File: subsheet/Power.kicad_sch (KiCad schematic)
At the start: 27 parts, among them J501 Barrel_Jack, J502 PWR_IN, J503 ALTERNATE, Q501 DTC114E, Q502 DTC114E, U501 TPS2552DBV, U502 TPS2552DBV

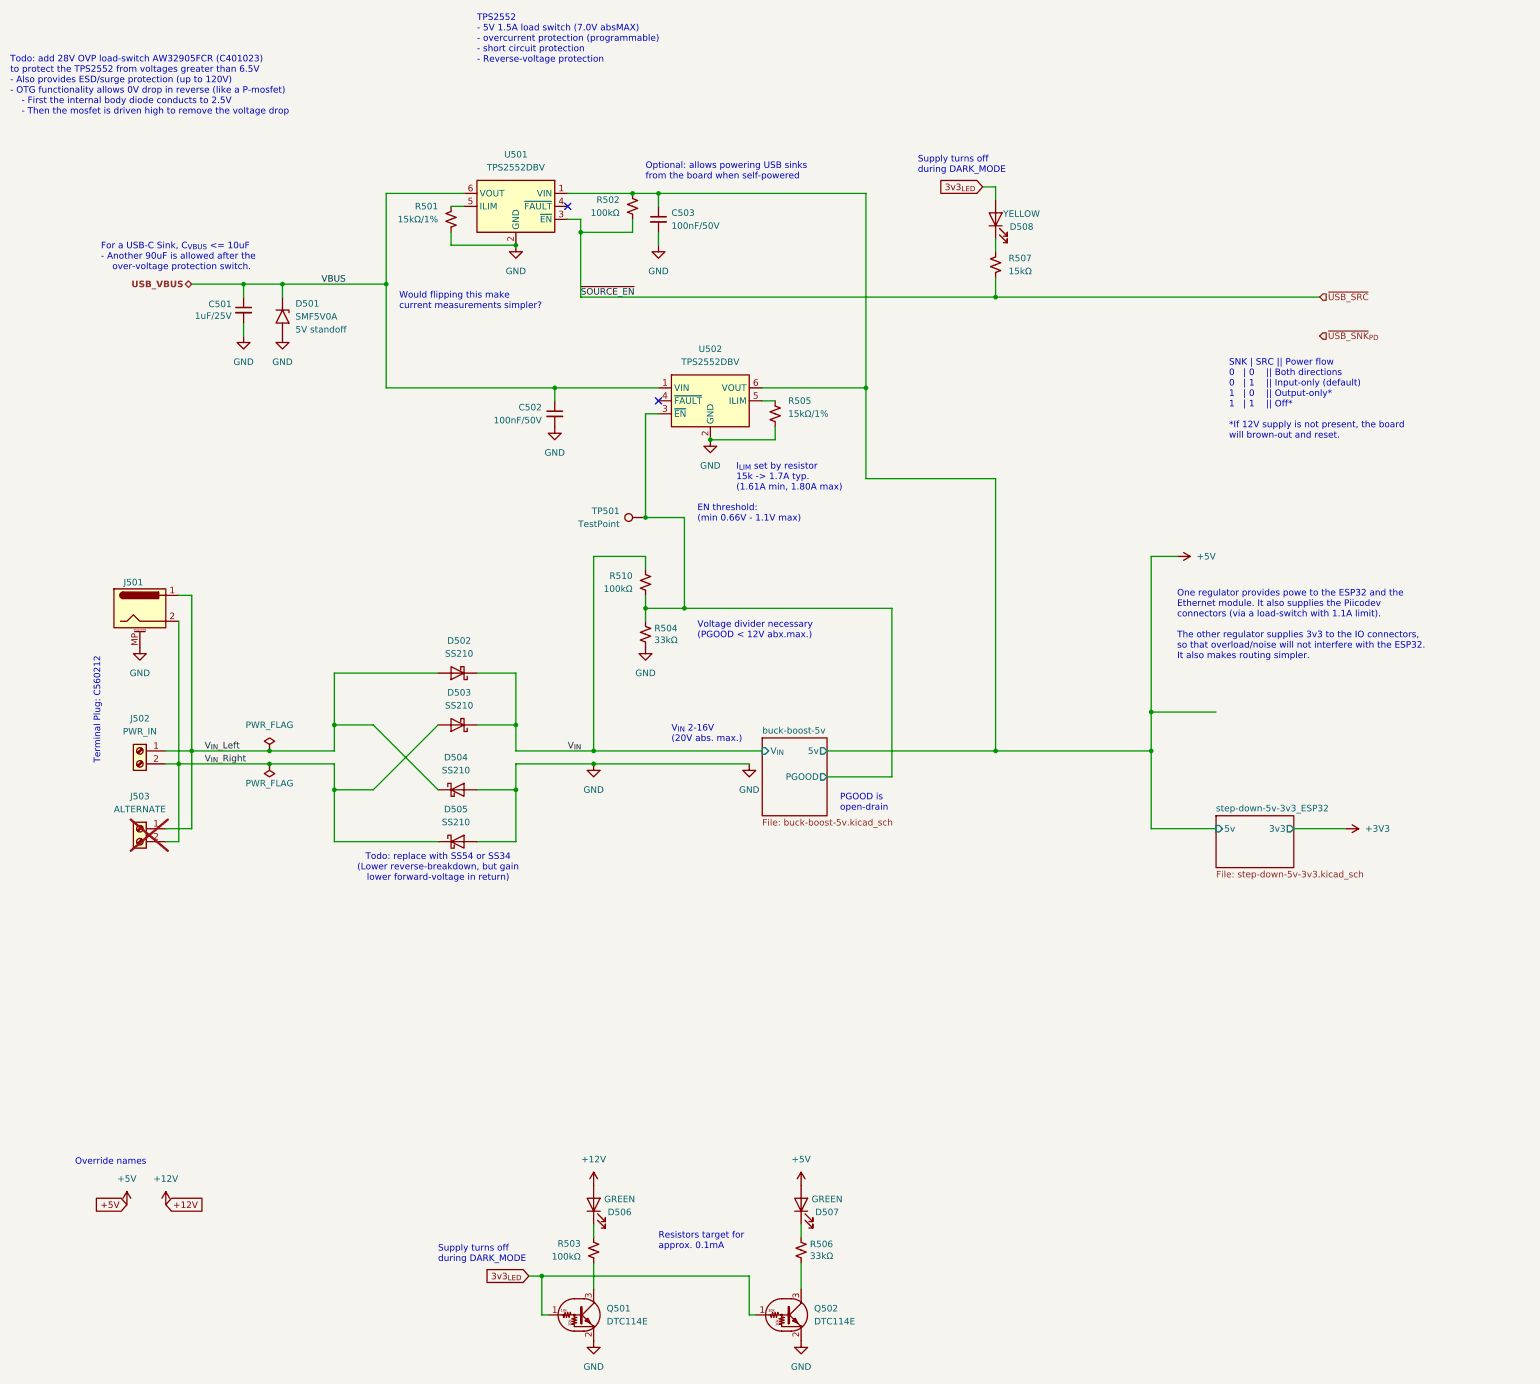
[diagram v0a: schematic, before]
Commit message: Removed USB-PD circuit - simplifies board
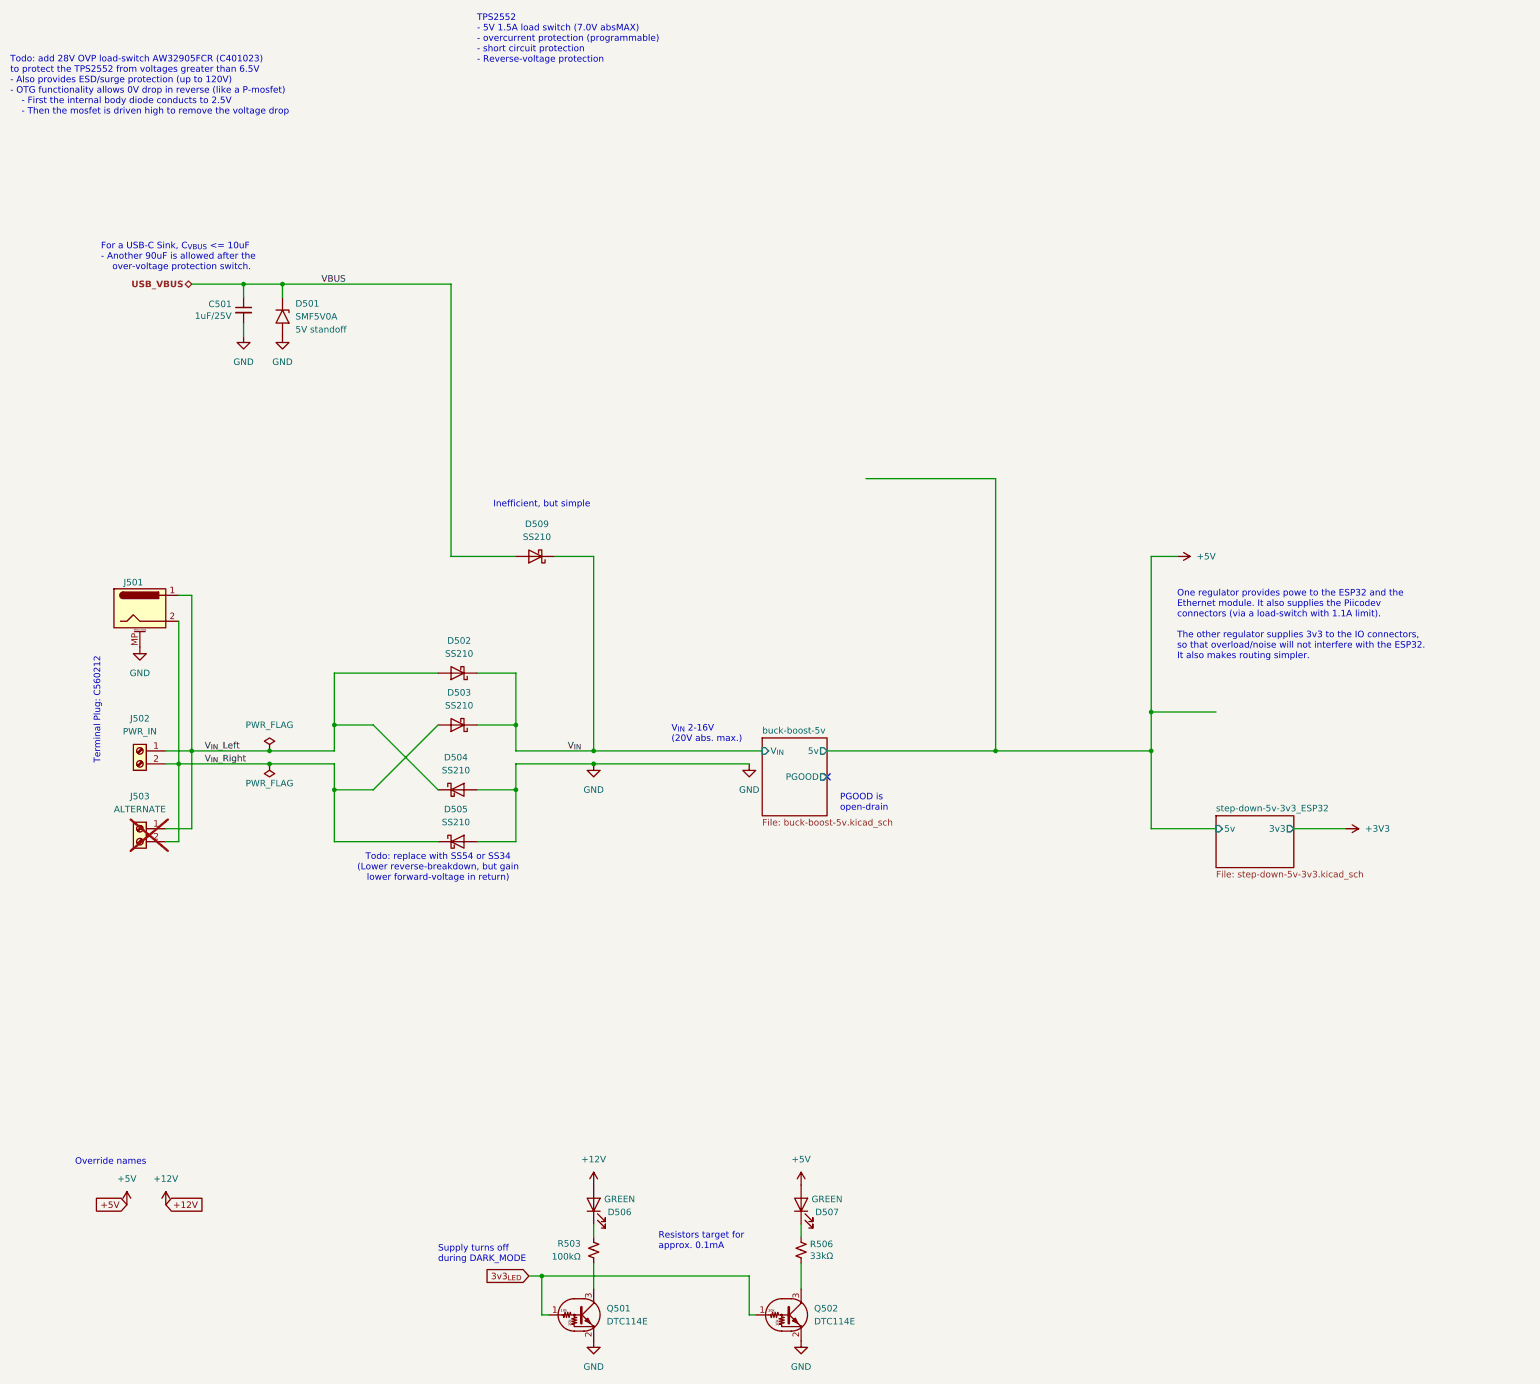
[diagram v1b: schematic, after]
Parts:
- removed C502, C503: 100nF/50V, Capacitor_SMD:C_0603_1608Metric, symbol Device:C_Small
- removed D508: YELLOW, LED_SMD:LED_0603_1608Metric, symbol Device:LED
- removed R501, R505: 15kΩ/1%, Resistor_SMD:R_0603_1608Metric, symbol Device:R_Small_US
- removed R502, R510: 100kΩ, Resistor_SMD:R_0603_1608Metric, symbol Device:R_Small_US
- removed R504: 33kΩ, Resistor_SMD:R_0603_1608Metric, symbol Device:R_Small_US
- removed R507: 15kΩ, Resistor_SMD:R_0603_1608Metric, symbol Device:R_Small_US
- removed TP501: TestPoint, symbol Connector:TestPoint
- removed U501, U502: TPS2552DBV, Package_TO_SOT_SMD:SOT-23-6, symbol Power_Management_custom:TPS2552DBV
- added D509: SS210, Diode_SMD:D_SMA, symbol Device:D_Schottky
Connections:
- net USB_VBUS: now also D509.2 (A)
- net V_{IN}: now also D509.1 (K)
- no-connect marks 2 -> 1
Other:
- note added: "Inefficient, but simple"
- note removed: "EN threshold: (min 0.66V - 1.1V max)"
- note removed: "I_{LIM} set by resistor 15k -> 1.7A typ. (1.61A min, 1.80A max)"
- note removed: "Optional: allows powering USB sinks from the board when self-powered"
- note removed: "SNK | SRC || Power flow 0 | 0 || Both directions 0 | 1 || Input-only (default) 1 | 0 || Output-only* 1 | 1 || Off* *If 12V supply is not present, the board will brown-out and reset."
- note removed: "Voltage divider necessary (PGOOD < 12V abx.max.)"
- note removed: "Would flipping this make current measurements simpler?"

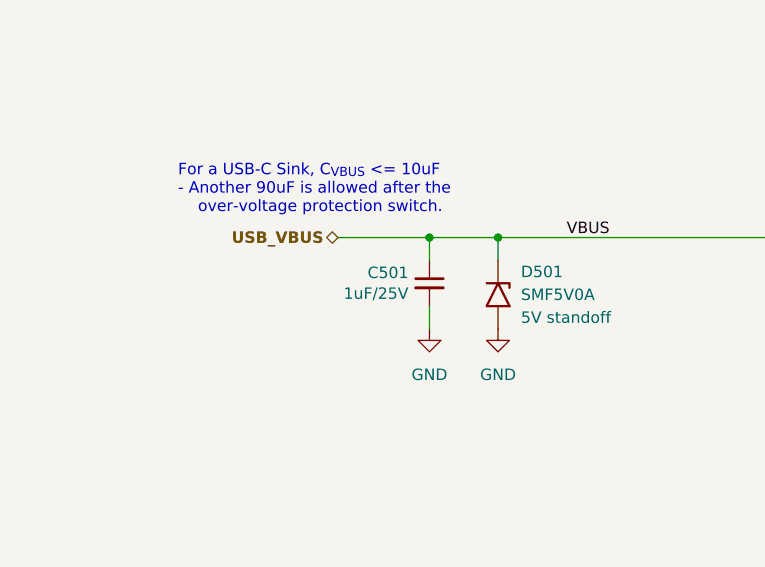
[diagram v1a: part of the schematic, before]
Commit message: Planning/wiring up some traces on PCB
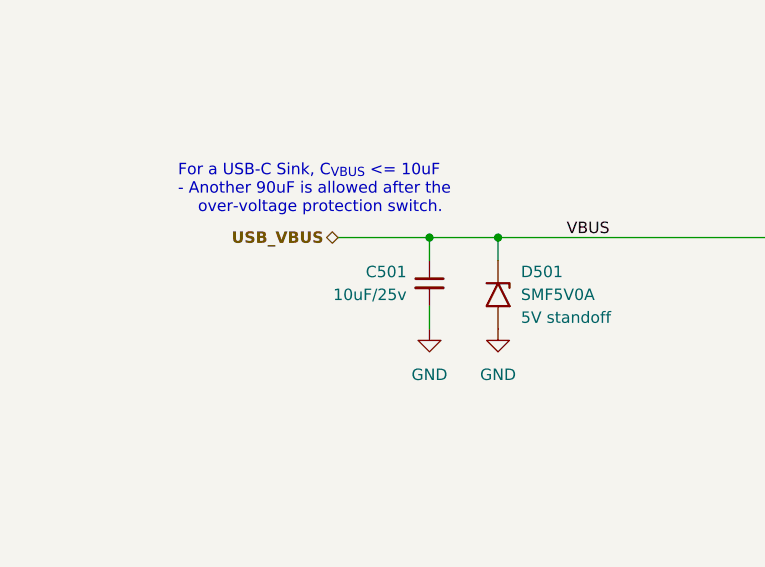
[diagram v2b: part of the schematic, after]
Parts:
- C501: value 1uF/25V -> 10uF/25v; footprint Capacitor_SMD:C_0402_1005Metric -> Capacitor_SMD:C_0603_1608Metric; LCSC C52923 -> C96446
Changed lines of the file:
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@@
+	)
+	(symbol
+		(lib_id "Device:C_Small")
+		(at 43.18 45.72 0)
+		(unit 1)
+		(exclude_from_sim no)
+		(in_bom yes)
+		(on_board yes)
+		(dnp no)
+		(fields_autoplaced yes)
+		(property "Reference" "C501"
+			(at 40.64 44.4562 0)
+			(effects
+				(font
+					(size 1.27 1.27)
+				)
+				(justify right)
+			)
+		)
+		(property "Value" "10uF/25v"
+			(at 40.64 46.9962 0)
+			(effects
+				(font
+					(size 1.27 1.27)
+				)
+				(justify right)
+			)
+		)
+		(property "Footprint" "Capacitor_SMD:C_0603_1608Metric"
+			(at 43.18 45.72 0)
+			(effects
+				(font
+					(size 1.27 1.27)
+				)
+				(hide yes)
+			)
+		)
+		(property "Datasheet" "~"
+			(at 43.18 45.72 0)
+			(effects
+				(font
+					(size 1.27 1.27)
+				)
+				(hide yes)
+			)
+		)
+		(property "Description" ""
+			(at 43.18 45.72 0)
+			(effects
+				(font
+					(size 1.27 1.27)
+				)
+				(hide yes)
+			)
+		)
+		(property "LCSC" "C96446"
+			(at 43.18 45.72 0)
+			(effects
+				(font
+					(size 1.27 1.27)
+				)
+				(hide yes)
+			)
+		)
+		(pin "1"
+		)
+		(pin "2"
+		)
+		(instances
+			(project "ESP_bare_chip_test_board"
+				(path "/45b6f84a-e69b-48be-a49b-bc68872e2c15/28425a28-8968-4679-b18b-58814452f93f"
+					(reference "C501")
+					(unit 1)
+				)
+			)
+		)
 	)
 	(symbol
@@
 					(unit 1)
 				)
-			)
-		)
-	)
-	(symbol
-		(lib_id "Device:C_Small")
-		(at 43.18 45.72 0)
-		(unit 1)
-		(exclude_from_sim no)
-		(in_bom yes)
-		(on_board yes)
-		(dnp no)
-		(property "Reference" "C501"
-			(at 40.8432 44.5516 0)
-			(effects
-				(font
-					(size 1.27 1.27)
-				)
-				(justify right)
-			)
-		)
-		(property "Value" "1uF/25V"
-			(at 40.8432 46.863 0)
-			(effects
-				(font
-					(size 1.27 1.27)
-				)
-				(justify right)
-			)
-		)
-		(property "Footprint" "Capacitor_SMD:C_0402_1005Metric"
-			(at 43.18 45.72 0)
-			(effects
-				(font
-					(size 1.27 1.27)
-				)
-				(hide yes)
-			)
-		)
-		(property "Datasheet" "~"
-			(at 43.18 45.72 0)
-			(effects
-				(font
-					(size 1.27 1.27)
-				)
-				(hide yes)
-			)
-		)
-		(property "Description" ""
-			(at 43.18 45.72 0)
-			(effects
-				(font
-					(size 1.27 1.27)
-				)
-				(hide yes)
-			)
-		)
-		(property "LCSC" "C52923"
-			(at 43.18 45.72 0)
-			(effects
-				(font
-					(size 1.27 1.27)
-				)
-				(hide yes)
-			)
-		)
-		(pin "1"
-		)
-		(pin "2"
-		)
-		(instances
-			(project "ESP_bare_chip_test_board"
-				(path "/45b6f84a-e69b-48be-a49b-bc68872e2c15/28425a28-8968-4679-b18b-58814452f93f"
-					(reference "C501")
-					(unit 1)
-				)

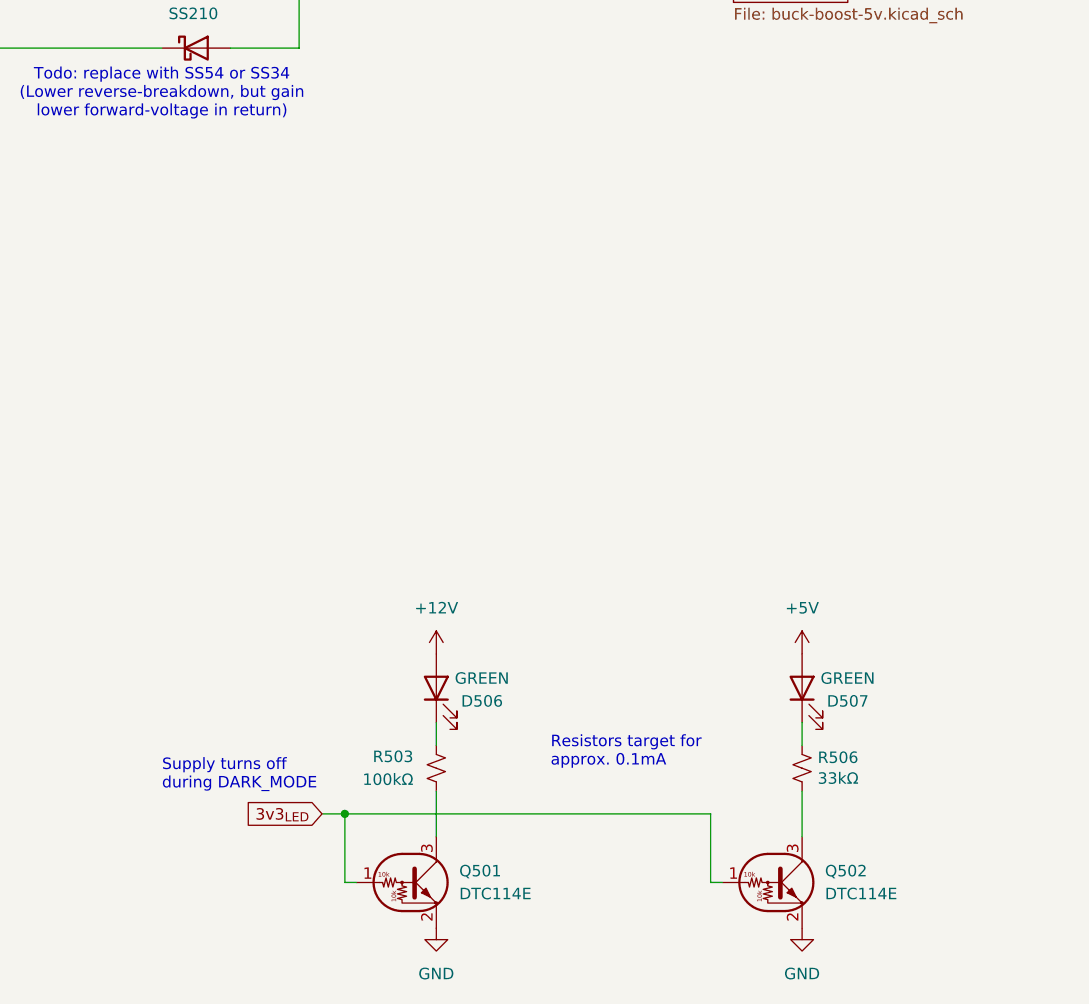
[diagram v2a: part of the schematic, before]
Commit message: Position final few components
Removed one ESD diode arrray - experimental board, so not really needed,
with the exception of the USB lines.

Add and position 5V indicator LED

Finished wiring up the 5V buck-boost regulator
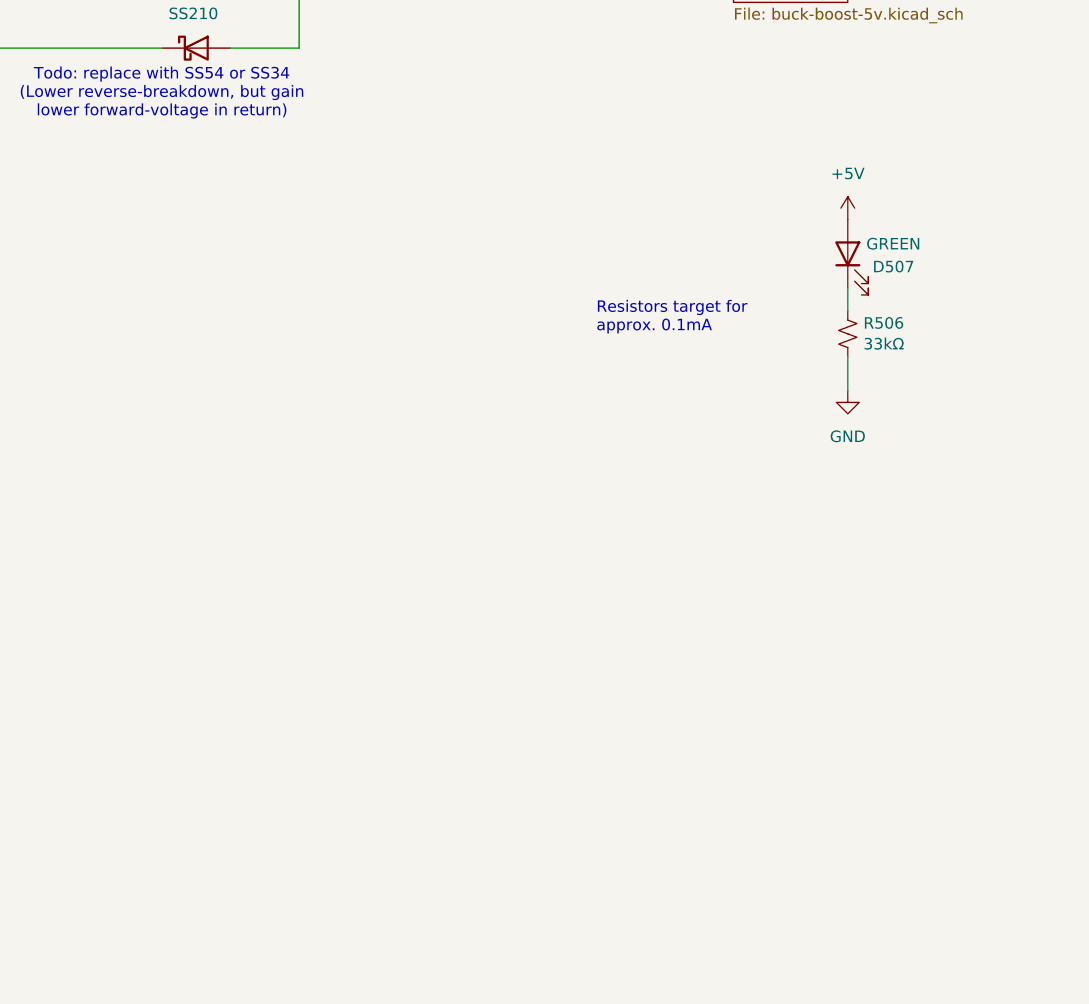
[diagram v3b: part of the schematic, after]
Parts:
- removed D506: GREEN, LED_SMD:LED_0603_1608Metric, symbol Device:LED
- removed Q501, Q502: DTC114E, Package_TO_SOT_SMD:SOT-323_SC-70, symbol Transistor_BJT:DTC114E
- removed R503: 100kΩ, Resistor_SMD:R_0603_1608Metric, symbol Device:R_Small_US
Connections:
- net GND: now also R506.2
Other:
- note removed: "Supply turns off during DARK_MODE"
- moved on the sheet: D507, R506

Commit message: Add order codes for all components
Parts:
- J501: JLCPCB_IGNORE (none) -> 1
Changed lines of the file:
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@@
+			)
+		)
+		(property "I2C address" ""
+			(at 85.09 139.7 0)
+			(effects
+				(font
+					(size 1.27 1.27)
+				)
+				(hide yes)
 			)
 		)
@@
 			)
 		)
+		(property "I2C address" ""
+			(at 50.8 46.99 0)
+			(effects
+				(font
+					(size 1.27 1.27)
+				)
+				(hide yes)
+			)
+		)
 		(pin "2"
 		)
@@
 			)
 		)
+		(property "I2C address" ""
+			(at 43.18 45.72 0)
+			(effects
+				(font
+					(size 1.27 1.27)
+				)
+				(hide yes)
+			)
+		)
 		(pin "1"
 		)
@@
 		)
 		(property "LCSC" "C14996"
+			(at 100.33 93.98 0)
+			(effects
+				(font
+					(size 1.27 1.27)
+				)
+				(hide yes)
+			)
+		)
+		(property "I2C address" ""
 			(at 100.33 93.98 0)
 			(effects
@@
 			)
 		)
+		(property "I2C address" ""
+			(at 22.86 147.32 0)
+			(effects
+				(font
+					(size 1.27 1.27)
+				)
+				(hide yes)
+			)
+		)
 		(pin "1"
 		)
@@
 			)
 		)
+		(property "I2C address" ""
+			(at 85.09 149.86 0)
+			(effects
+				(font
+					(size 1.27 1.27)
+				)
+				(hide yes)
+			)
+		)
 		(pin "1"
 		)
@@
 			)
 		)
+		(property "I2C address" ""
+			(at 22.86 104.14 0)
+			(effects
+				(font
+					(size 1.27 1.27)
+				)
+				(hide yes)
+			)
+		)
+		(property "JLCPCB_IGNORE" "1"
+			(at 22.86 104.14 0)
+			(effects
+				(font
+					(size 1.27 1.27)
+				)
+				(hide yes)
+			)
+		)
 		(pin "1"
 		)
@@
 		)
 		(property "JLCPCB_CORRECTION" "0;0;0"
+			(at 157.48 172.72 0)
+			(effects
+				(font
+					(size 1.27 1.27)
+				)
+				(hide yes)
+			)
+		)
+		(property "I2C address" ""
 			(at 157.48 172.72 0)
 			(effects
@@
 			)
 		)
+		(property "I2C address" ""
+			(at 22.86 132.08 0)
+			(effects
+				(font
+					(size 1.27 1.27)
+				)
+				(hide yes)
+			)
+		)
 		(pin "1"
 		)
@@
 			)
 		)
+		(property "I2C address" ""
+			(at 85.09 116.84 0)
+			(effects
+				(font
+					(size 1.27 1.27)
+				)
+				(hide yes)
+			)
+		)
 		(pin "1"
 		)
@@
 			)
 		)
+		(property "I2C address" ""
+			(at 157.48 181.61 0)
+			(effects
+				(font
+					(size 1.27 1.27)
+				)
+				(hide yes)
+			)
+		)
 		(pin "1"
 		)
@@
 			(at 85.09 127 0)
 			(effects
+				(font
+					(size 1.27 1.27)
+				)
+				(hide yes)
+			)
+		)
+		(property "I2C address" ""
+			(at 85.09 127 0)
+			(effects

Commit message: Add JLCPCB corrections for new components
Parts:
- D501: LCSC C1972946 -> C2905637
- J502, J503: JLCPCB_IGNORE (none) -> 1
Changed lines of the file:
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@@
 			)
 		)
-		(property "LCSC" "C1972946"
+		(property "LCSC" "C2905637"
 			(at 50.8 46.99 0)
 			(effects
@@
 			)
 		)
-		(property "JLCPCB_IGNORE" ""
+		(property "JLCPCB_IGNORE" "1"
 			(at 22.86 147.32 0)
 			(effects
@@
 			)
 		)
-		(property "JLCPCB_IGNORE" ""
+		(property "JLCPCB_IGNORE" "1"
 			(at 22.86 132.08 0)
 			(effects
